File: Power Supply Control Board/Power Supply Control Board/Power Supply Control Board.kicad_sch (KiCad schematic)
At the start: 50 parts, among them J1 Conn_01x12, Q1 BC546, Q2 BC546, Q3 MPSA92, Q4 BC546, U1 IR2153, U2 LM311, U3 LM311

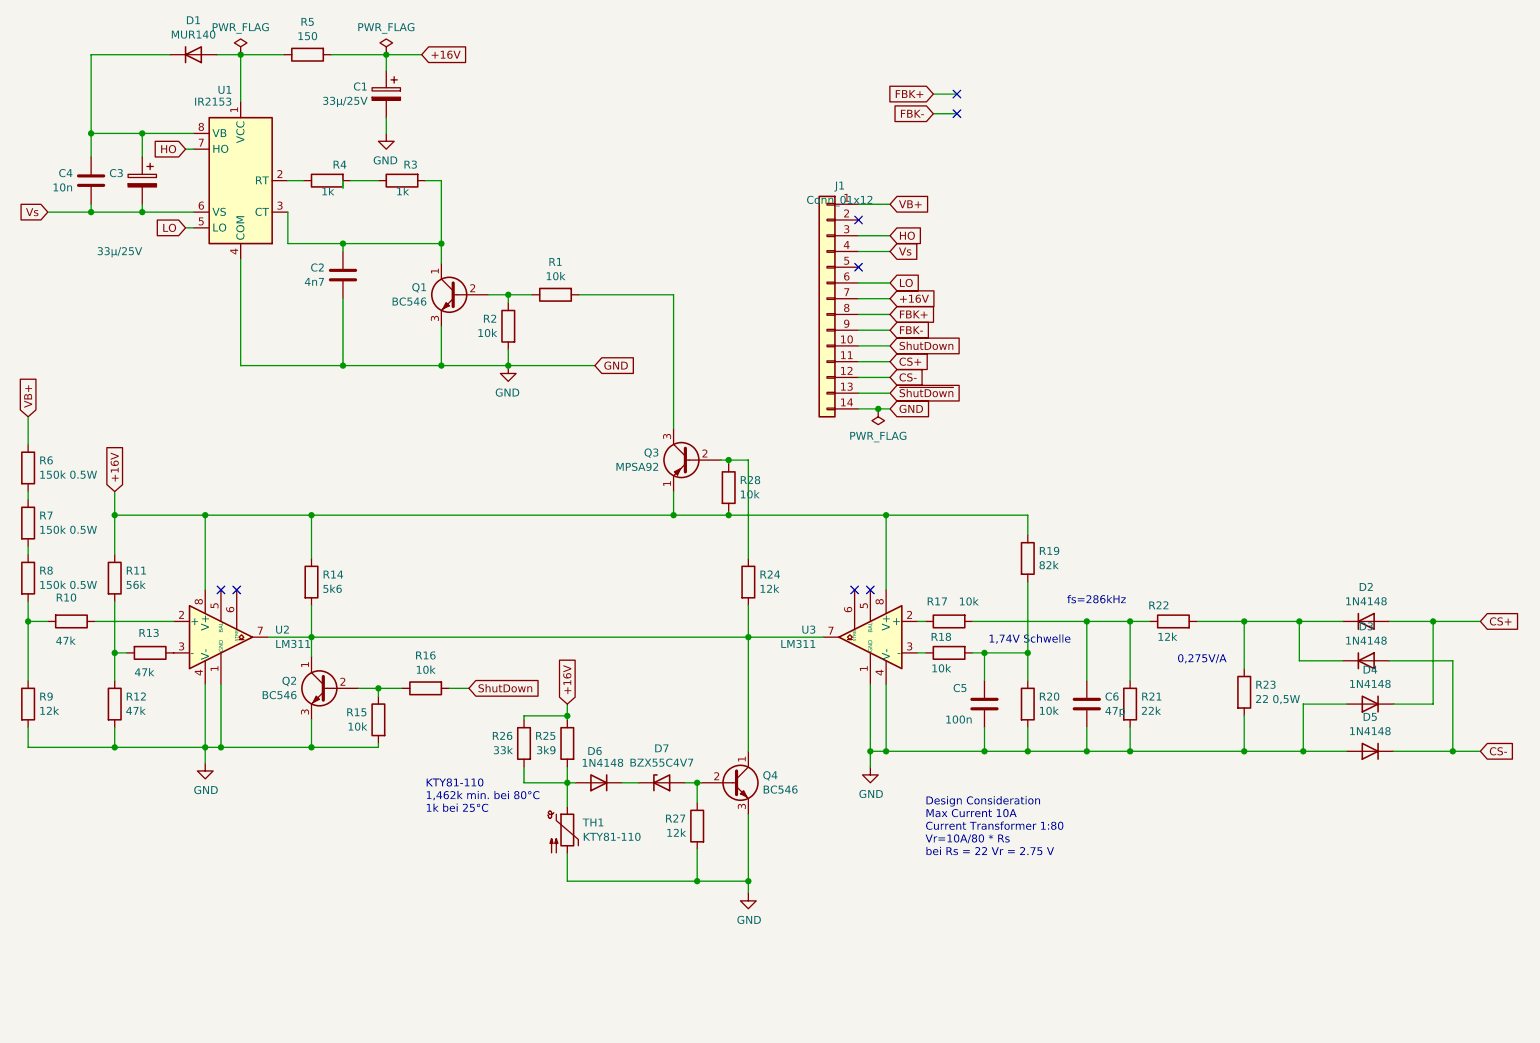
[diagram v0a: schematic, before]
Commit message: Add Top Layer Zones and some graphics to Main Board V2.0
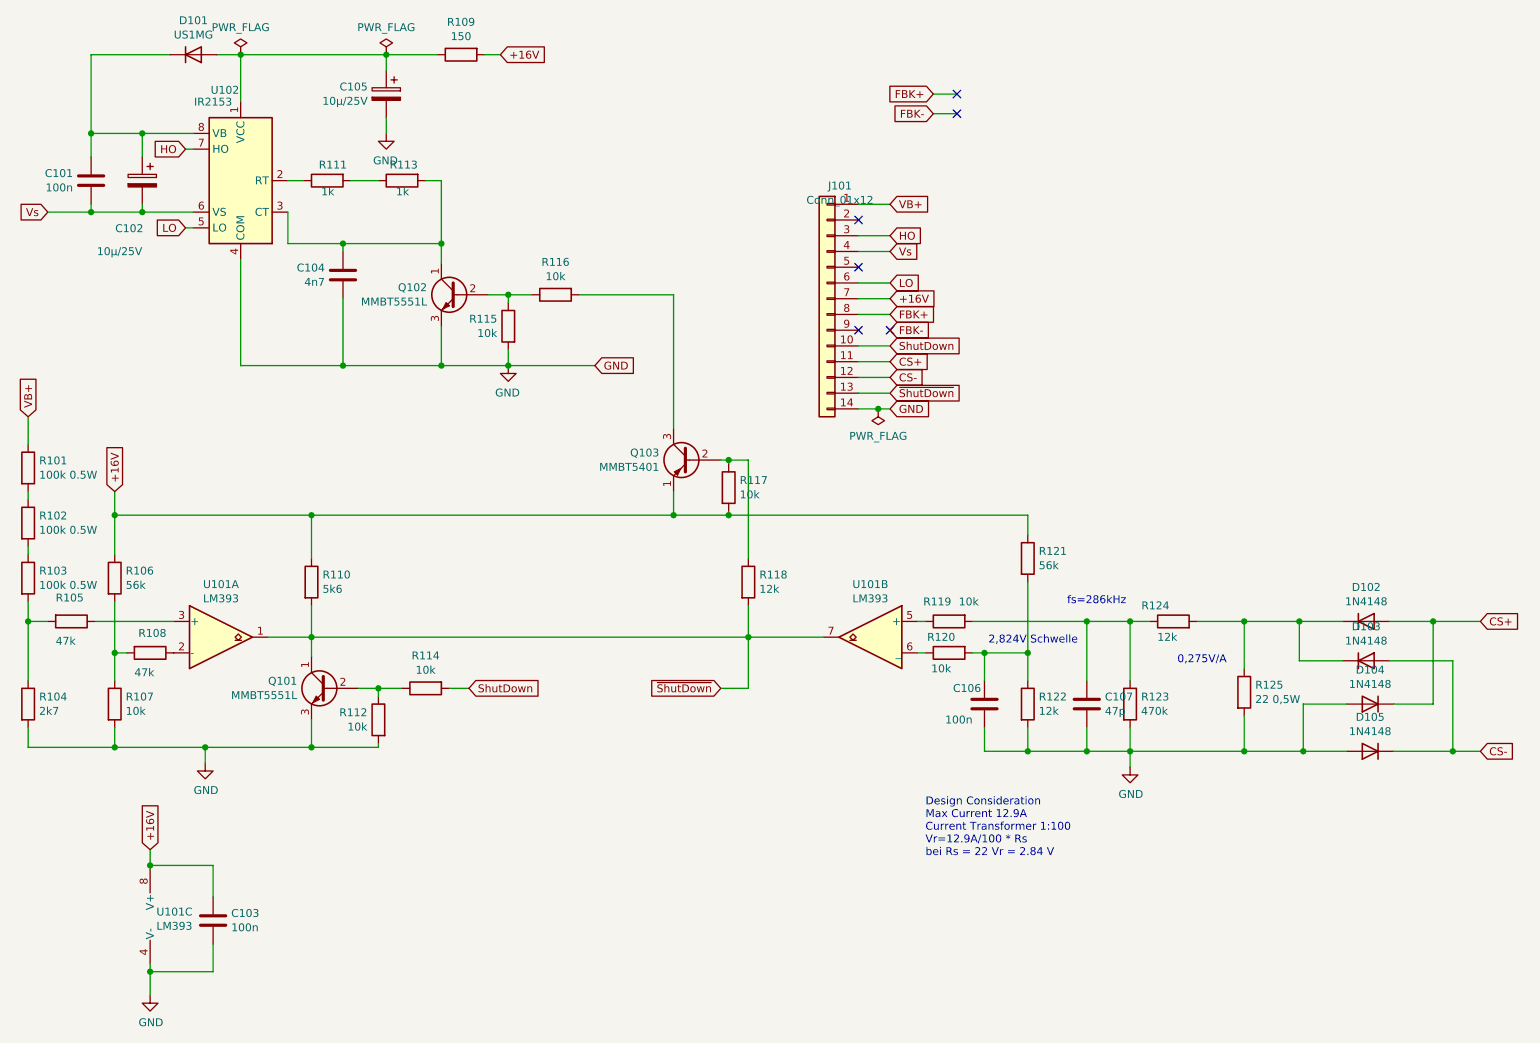
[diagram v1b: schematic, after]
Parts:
- removed D6: 1N4148, Diode_THT:D_DO-35_SOD27_P2.54mm_Vertical_AnodeUp, symbol Diode:1N4148
- removed D7: BZX55C4V7, Diode_THT:D_DO-35_SOD27_P2.54mm_Vertical_AnodeUp, symbol Diode:BZX84Cxx
- removed Q2, Q4: BC546, Package_TO_SOT_THT:TO-92_Inline, symbol Transistor_BJT:BC546
- removed R25: 3k9, Resistor_THT:R_Axial_DIN0207_L6.3mm_D2.5mm_P2.54mm_Vertical, symbol Device:R
- removed R26: 33k, Resistor_THT:R_Axial_DIN0207_L6.3mm_D2.5mm_P2.54mm_Vertical, symbol Device:R
- removed R27: 12k, Resistor_THT:R_Axial_DIN0207_L6.3mm_D2.5mm_P2.54mm_Vertical, symbol Device:R
- removed TH1: KTY81-110, Package_TO_SOT_THT:SOD-70_P5.08mm, symbol Sensor_Temperature:KTY81
- removed U2, U3: LM311, Package_DIP:DIP-8_W7.62mm_LongPads, symbol Comparator:LM311
- added C103: 100n, Capacitor_SMD:C_0805_2012Metric, symbol Device:C
- added Q101: MMBT5551L, Package_TO_SOT_SMD:SOT-23, symbol Transistor_BJT:BC546
- added U101: LM393, Package_SO:SOIC-8_3.9x4.9mm_P1.27mm, symbol Comparator:LM393
- C101: renamed from C4; value 10n -> 100n; footprint Capacitor_THT:C_Rect_L7.2mm_W3.0mm_P5.00mm_FKS2_FKP2_MKS2_MKP2 -> Capacitor_SMD:C_0805_2012Metric
- C102: renamed from C3; value 33µ/25V -> 10µ/25V; footprint Capacitor_THT:CP_Radial_D7.5mm_P2.50mm -> Capacitor_SMD:C_0805_2012Metric
- C104: renamed from C2; footprint Capacitor_THT:C_Rect_L7.2mm_W3.0mm_P5.00mm_FKS2_FKP2_MKS2_MKP2 -> Capacitor_SMD:C_0805_2012Metric
- C105: renamed from C1; value 33µ/25V -> 10µ/25V; footprint Capacitor_THT:CP_Radial_D7.5mm_P2.50mm -> Capacitor_SMD:C_0805_2012Metric
- C106: renamed from C5; footprint Capacitor_THT:C_Rect_L7.2mm_W3.0mm_P5.00mm_FKS2_FKP2_MKS2_MKP2 -> Capacitor_SMD:C_0805_2012Metric
- C107: renamed from C6; footprint Capacitor_THT:C_Disc_D4.7mm_W2.5mm_P5.00mm -> Capacitor_SMD:C_0402_1005Metric
- D101: renamed from D1; value MUR140 -> US1MG; footprint Diode_THT:D_DO-34_SOD68_P2.54mm_Vertical_AnodeUp -> Diode_SMD:D_SMA
- D102: renamed from D2; footprint Diode_THT:D_DO-35_SOD27_P2.54mm_Vertical_AnodeUp -> Diode_SMD:D_SOD-123
- D103: renamed from D3; footprint Diode_THT:D_DO-35_SOD27_P2.54mm_Vertical_AnodeUp -> Diode_SMD:D_SOD-123
- D104: renamed from D4; footprint Diode_THT:D_DO-35_SOD27_P2.54mm_Vertical_AnodeUp -> Diode_SMD:D_SOD-123
- D105: renamed from D5; footprint Diode_THT:D_DO-35_SOD27_P2.54mm_Vertical_AnodeUp -> Diode_SMD:D_SOD-123
- Q102: renamed from Q1; value BC546 -> MMBT5551L; footprint Package_TO_SOT_THT:TO-92_Inline -> Package_TO_SOT_SMD:SOT-23
- Q103: renamed from Q3; value MPSA92 -> MMBT5401; footprint Package_TO_SOT_THT:TO-92_Inline -> Package_TO_SOT_SMD:SOT-23
- R101: renamed from R6; value 150k 0.5W -> 100k 0.5W; footprint Resistor_THT:R_Axial_DIN0309_L9.0mm_D3.2mm_P5.08mm_Vertical -> Resistor_SMD:R_1206_3216Metric
- R102: renamed from R7; value 150k 0.5W -> 100k 0.5W; footprint Resistor_THT:R_Axial_DIN0309_L9.0mm_D3.2mm_P5.08mm_Vertical -> Resistor_SMD:R_1206_3216Metric
- R103: renamed from R8; value 150k 0.5W -> 100k 0.5W; footprint Resistor_THT:R_Axial_DIN0309_L9.0mm_D3.2mm_P5.08mm_Vertical -> Resistor_SMD:R_1206_3216Metric
- R104: renamed from R9; value 12k -> 2k7; footprint Resistor_THT:R_Axial_DIN0207_L6.3mm_D2.5mm_P2.54mm_Vertical -> Resistor_SMD:R_0805_2012Metric
- R105: renamed from R10; footprint Resistor_THT:R_Axial_DIN0207_L6.3mm_D2.5mm_P2.54mm_Vertical -> Resistor_SMD:R_0805_2012Metric
- R106: renamed from R11; footprint Resistor_THT:R_Axial_DIN0207_L6.3mm_D2.5mm_P2.54mm_Vertical -> Resistor_SMD:R_0805_2012Metric
- R107: renamed from R12; value 47k -> 10k; footprint Resistor_THT:R_Axial_DIN0207_L6.3mm_D2.5mm_P2.54mm_Vertical -> Resistor_SMD:R_0805_2012Metric
- R108: renamed from R13; footprint Resistor_THT:R_Axial_DIN0207_L6.3mm_D2.5mm_P2.54mm_Vertical -> Resistor_SMD:R_0805_2012Metric
- R109: renamed from R5; footprint Resistor_THT:R_Axial_DIN0207_L6.3mm_D2.5mm_P2.54mm_Vertical -> Resistor_SMD:R_0805_2012Metric
- R110: renamed from R14; footprint Resistor_THT:R_Axial_DIN0207_L6.3mm_D2.5mm_P2.54mm_Vertical -> Resistor_SMD:R_0805_2012Metric
- R111: renamed from R4; footprint Resistor_THT:R_Axial_DIN0207_L6.3mm_D2.5mm_P2.54mm_Vertical -> Resistor_SMD:R_0805_2012Metric
- R112: renamed from R15; footprint Resistor_THT:R_Axial_DIN0207_L6.3mm_D2.5mm_P2.54mm_Vertical -> Resistor_SMD:R_0805_2012Metric
- R113: renamed from R3; footprint Resistor_THT:R_Axial_DIN0207_L6.3mm_D2.5mm_P2.54mm_Vertical -> Resistor_SMD:R_0805_2012Metric
- R114: renamed from R16; footprint Resistor_THT:R_Axial_DIN0207_L6.3mm_D2.5mm_P2.54mm_Vertical -> Resistor_SMD:R_0805_2012Metric
- R115: renamed from R2; footprint Resistor_THT:R_Axial_DIN0207_L6.3mm_D2.5mm_P2.54mm_Vertical -> Resistor_SMD:R_0805_2012Metric
- R116: renamed from R1; footprint Resistor_THT:R_Axial_DIN0207_L6.3mm_D2.5mm_P2.54mm_Vertical -> Resistor_SMD:R_0805_2012Metric
- R117: renamed from R28; footprint Resistor_THT:R_Axial_DIN0207_L6.3mm_D2.5mm_P2.54mm_Vertical -> Resistor_SMD:R_0805_2012Metric
- R118: renamed from R24; footprint Resistor_THT:R_Axial_DIN0207_L6.3mm_D2.5mm_P2.54mm_Vertical -> Resistor_SMD:R_0805_2012Metric
- R119: renamed from R17; footprint Resistor_THT:R_Axial_DIN0207_L6.3mm_D2.5mm_P2.54mm_Vertical -> Resistor_SMD:R_0805_2012Metric
- R120: renamed from R18; footprint Resistor_THT:R_Axial_DIN0207_L6.3mm_D2.5mm_P2.54mm_Vertical -> Resistor_SMD:R_0805_2012Metric
- R121: renamed from R19; value 82k -> 56k; footprint Resistor_THT:R_Axial_DIN0207_L6.3mm_D2.5mm_P2.54mm_Vertical -> Resistor_SMD:R_0805_2012Metric
- R122: renamed from R20; value 10k -> 12k; footprint Resistor_THT:R_Axial_DIN0207_L6.3mm_D2.5mm_P2.54mm_Vertical -> Resistor_SMD:R_0805_2012Metric
- R123: renamed from R21; value 22k -> 470k; footprint Resistor_THT:R_Axial_DIN0207_L6.3mm_D2.5mm_P2.54mm_Vertical -> Resistor_SMD:R_0805_2012Metric
- R124: renamed from R22; footprint Resistor_THT:R_Axial_DIN0207_L6.3mm_D2.5mm_P2.54mm_Vertical -> Resistor_SMD:R_0805_2012Metric
- R125: renamed from R23; footprint Resistor_THT:R_Axial_DIN0309_L9.0mm_D3.2mm_P5.08mm_Vertical -> Resistor_SMD:R_1206_3216Metric
- U102: renamed from U1; footprint Package_DIP:DIP-8_W7.62mm_LongPads -> Package_SO:SOIC-8_3.9x4.9mm_P1.27mm; LCSC (none) -> C79666
- renumbered J1 to J101
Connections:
- net +16V: now also C103.1, U101.8 (V+); no longer C105.1
- net FBK-: no longer J101.9 (Pin_9)
- net GND: now also C103.2, Q101.3 (E), U101.4 (V-)
- net ~ShutDown: now also R110.2, R118.2, Q101.1 (C), U101.1, U101.7
- net at R105.1: now also U101.3 (+)
- net at R108.1: now also U101.2 (-)
- net at R119.1: now also U101.5 (+)
- net at R120.1: now also U101.6 (_)
- net at R112.1, R114.1: now also Q101.2 (B)
- net at D101.2 (A), R109.1, U102.1 (VCC): now also C105.1
- no-connect marks 8 -> 6
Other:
- note added: "2,824V Schwelle"
- note added: "Design Consideration Max Current 12.9A Current Transformer 1:100 Vr=12.9A/100 * Rs bei Rs = 22 Vr = 2.84 V"
- note removed: "1,74V Schwelle"
- note removed: "Design Consideration Max Current 10A Current Transformer 1:80 Vr=10A/80 * Rs bei Rs = 22 Vr = 2.75 V"
- note removed: "KTY81-110 1,462k min. bei 80°C 1k bei 25°C"
- moved on the sheet: R109
